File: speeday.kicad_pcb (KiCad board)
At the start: 4 copper layers, 100 x 100 mm, 238 parts, among them IC1 Trig Cond Socket, IC10 VNL5090N3-E, IC2 LM3940IMP-3.3_NOPB, IC3 VNL5090N3-E, IC4 VNL5090N3-E, IC5 VNL5090N3-E, IC6 VNL5090N3-E, IC7 VNL5090N3-E, IC8 VNL5090N3-E, IC9 VNL5090N3-E, J1 Conn_01x04, J10 Conn_02x02_Counter_Clockwise, J11 Conn_02x02_Counter_Clockwise, J12 Conn_02x02_Counter_Clockwise, J13 Conn_02x02_Counter_Clockwise, J14 Conn_02x02_Counter_Clockwise, J15 Conn_01x02, J16 Conn_01x02, J17 Conn_01x02, J18 Conn_01x02, J19 Conn_01x01, J2 Micro_SD_Card, J20 Conn_01x01, J21 Conn_01x01, J22 Conn_01x01, J23 Conn_01x02, J24 Conn_01x02, J25 Conn_01x08, J26 Conn_01x08, J27 Conn_01x04, J3 Conn_01x04, J4 Conn_01x02, J5 Conn_01x04, J6 Screw_Terminal_01x02, J7 Conn_02x02_Counter_Clockwise, J8 Conn_02x02_Counter_Clockwise, J9 Conn_02x02_Counter_Clockwise, P1 USB_C_Plug_USB2.0, Q1 SSM3K357R, Q2 SSM3K357R, Q3 SSM3K357R, Q4 SSM3K357R, SW1 SW_DIP_x01, SW2 SW_DIP_x01, SW3 SW_SPDT, U11 MCP2551-I-SN, U16 IXDN602, U17 IXDN602, U18 LM2940S-5.0/NOPB, U2 TXB0108PW, U3 TXB0108PW, U4 W25Q16JVSS, U5 MPX4250, U6 SP720, U7 STM32F407VGTx, Y1 Crystal_GND23

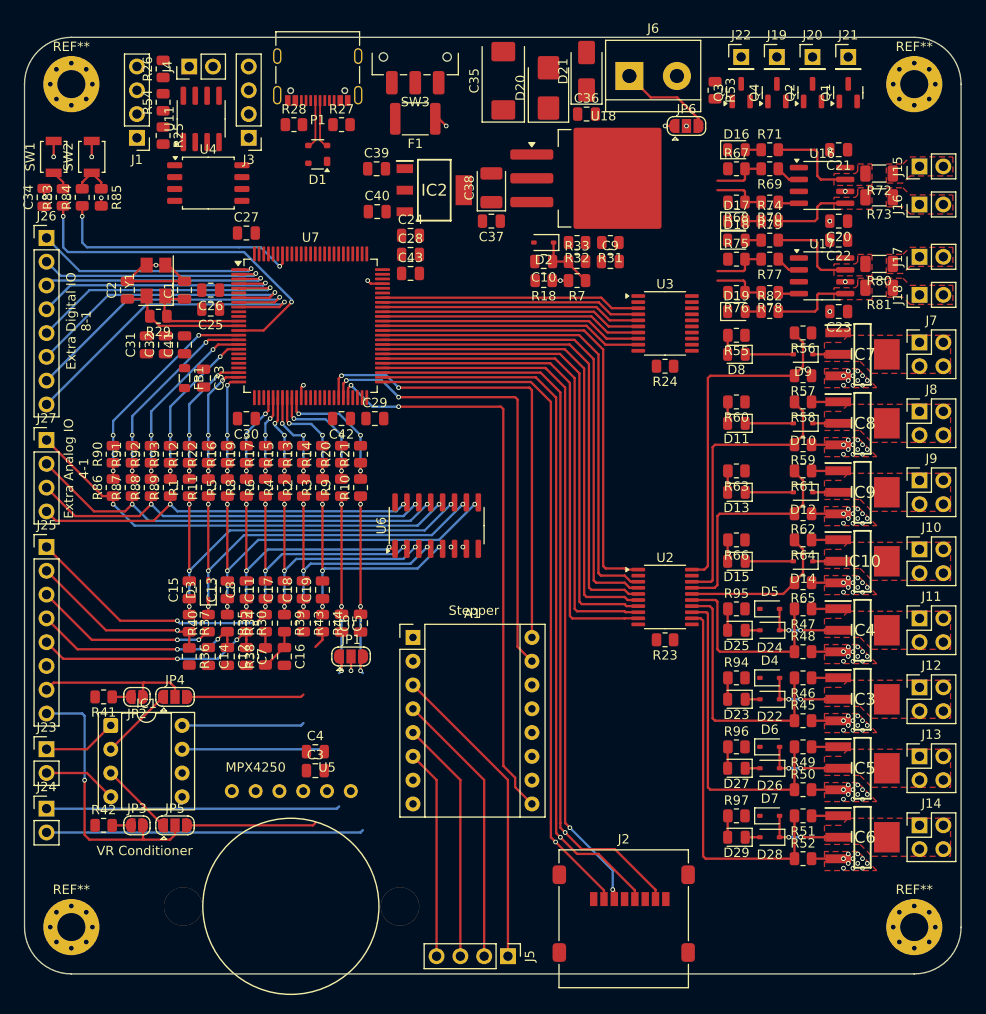
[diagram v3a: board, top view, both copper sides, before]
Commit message: Update from Speeduino Discord suggestions (thanks to Detonator)
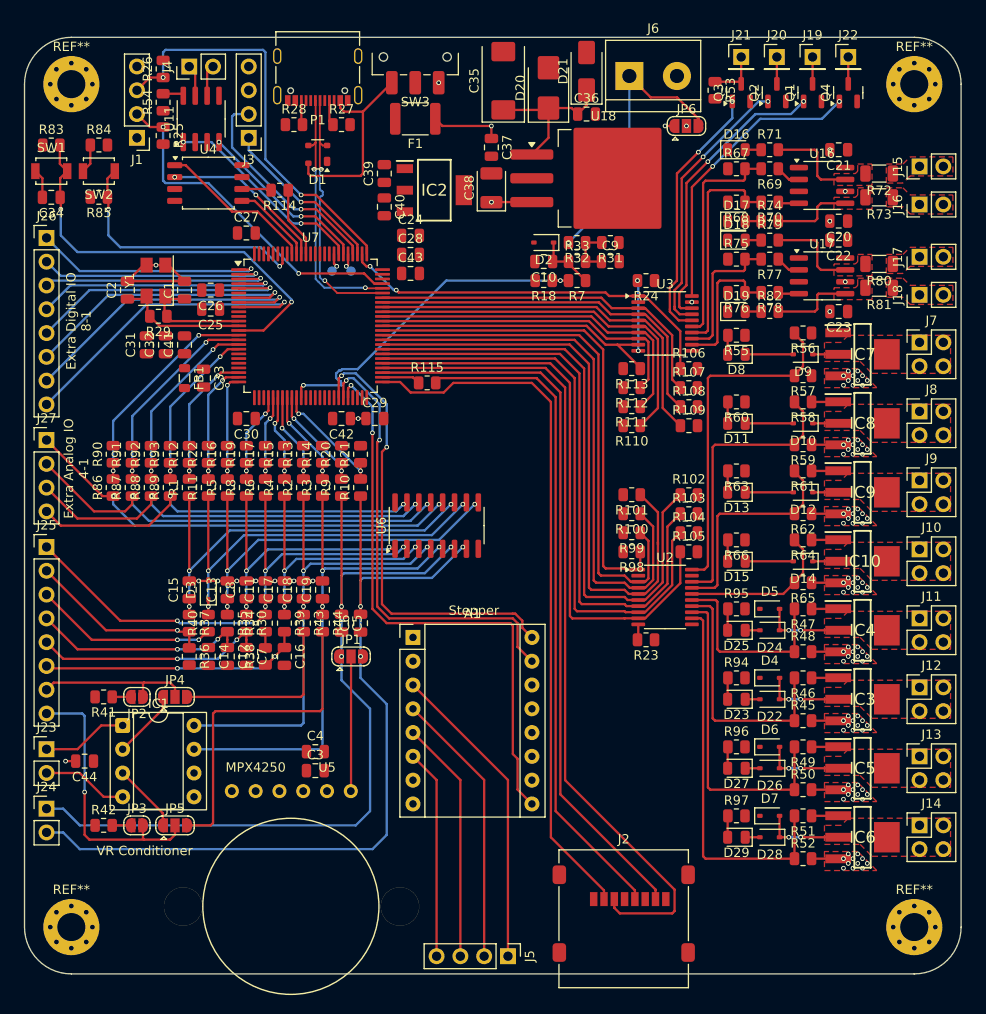
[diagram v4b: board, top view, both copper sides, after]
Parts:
- added C44: 100nF, Capacitor_SMD:C_0805_2012Metric, F.Cu at (26.4, 97.3)
- added R100: 51k, Resistor_SMD:R_0805_2012Metric, F.Cu at (84.8, 70.9)
- added R101: 51k, Resistor_SMD:R_0805_2012Metric, F.Cu at (84.8, 68.8)
- added R102: 51k, Resistor_SMD:R_0805_2012Metric, F.Cu at (90.9, 68.8)
- added R103: 51k, Resistor_SMD:R_0805_2012Metric, F.Cu at (90.9, 70.9)
- added R104: 51k, Resistor_SMD:R_0805_2012Metric, F.Cu at (90.9, 72.9)
- added R105: 51k, Resistor_SMD:R_0805_2012Metric, F.Cu at (90.9, 74.9)
- added R106: 51k, Resistor_SMD:R_0805_2012Metric, F.Cu at (90.9, 55.4)
- added R107: 51k, Resistor_SMD:R_0805_2012Metric, F.Cu at (90.9, 57.4)
- added R108: 51k, Resistor_SMD:R_0805_2012Metric, F.Cu at (90.9, 59.4)
- added R109: 51k, Resistor_SMD:R_0805_2012Metric, F.Cu at (90.9, 61.5)
- added R110: 51k, Resistor_SMD:R_0805_2012Metric, F.Cu at (84.8, 61.5)
- added R111: 51k, Resistor_SMD:R_0805_2012Metric, F.Cu at (84.8, 59.4)
- added R112: 51k, Resistor_SMD:R_0805_2012Metric, F.Cu at (84.8, 57.4)
- added R113: 51k, Resistor_SMD:R_0805_2012Metric, F.Cu at (84.8, 55.4)
- added R114: 22R, Resistor_SMD:R_0805_2012Metric, F.Cu at (47.2, 36.3)
- added R115: 22R, Resistor_SMD:R_0805_2012Metric, F.Cu at (63.0, 56.9)
- added R98: 51k, Resistor_SMD:R_0805_2012Metric, F.Cu at (84.8, 74.9)
- added R99: 51k, Resistor_SMD:R_0805_2012Metric, F.Cu at (84.8, 72.9)
- added TP1: TestPoint, TestPoint:TestPoint_Pad_D1.0mm, B.Cu at (52.8, 45.0)
- added TP2: TestPoint, TestPoint:TestPoint_Pad_D1.0mm, B.Cu at (54.9, 45.0)
- C10, C11, C13, C15, C17, C8: value 0.22uF -> 220nF
- C12, C14, C16, C19, C36, C37, C7, C9: value 0.1uF -> 100nF
- C18, C3: value 0.01uF -> 100nF
- C34: value C -> 100nF
- R84: value 10k -> 1k
- moved J21 11.4 mm to (96.5, 22.1)
- moved J22 11.4 mm to (108.0, 22.1)
- moved R24 9.37 mm to (86.4, 46.0)
- moved C37 7.87 mm to (69.8, 31.8), turned to -90 degrees
- moved Q4 7.62 mm to (108.0, 25.9)
- moved R84 5.86 mm to (27.9, 31.5), turned to 0 degrees
- moved R83 5.73 mm to (22.9, 31.5), turned to 0 degrees
- moved J19 3.81 mm to (104.1, 22.1)
- moved J20 3.81 mm to (100.3, 22.1)
- moved Q1 3.81 mm to (104.1, 25.9)
- moved Q2 3.81 mm to (100.3, 25.9)
- moved R23 2.03 mm to (86.4, 84.3)
- moved SW2 1.70 mm to (27.9, 34.3), turned to 180 degrees
- moved SW1 1.55 mm to (22.9, 34.3), turned to 0 degrees
- moved IC1 1.27 mm to (30.5, 93.5)
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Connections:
- C37 pad 1: 5V-REGULATOR -> +5V
- J2 pad 5: MCU-SPI-SD-CLK -> Net-(J2-CLK)
- R32 pad 2: +12V -> RAW-BAT
- R7 pad 1: RAW-BAT -> RAW-BAT-REF
- R83 pad 1: MCU_RESET -> +3.3V
- R83 pad 2: Net-(R83-Pad2) -> MCU_RESET
- R84 pad 1: MCU_BOOT -> Net-(R84-Pad1)
- R84 pad 2: Net-(R84-Pad2) -> +3.3V
- R85 pad 1: Net-(R84-Pad2) -> MCU_BOOT
- SW1 pad 1: Net-(R83-Pad2) -> GND
- SW1 pad 2: GND -> MCU_RESET
- SW2 pad 1: Net-(R84-Pad2) -> MCU_BOOT
- SW2 pad 2: +3.3V -> Net-(R84-Pad1)
- U3 pad 16: FAN-TRIG -> TACHO-TRIG
- U3 pad 18: TACHO-TRIG -> FAN-TRIG
- U3 pad 3: MCU-TACHO-TRIG-D -> MCU-FAN-TRIG-D
- U3 pad 5: MCU-FAN-TRIG-D -> MCU-TACHO-TRIG-D
- U4 pad 6: MCU-SPI-FLASH-CLK -> Net-(U4-CLK)
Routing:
- net MCU-SPI-SD-CLK: track 77.8 -> 4.11 mm, vias 1 -> 0
- net Net-(J2-CLK): track 0.00 -> 71.0 mm
- net MCU-SWD-CLK: track 0.00 -> 44.1 mm, vias 0 -> 2
- net MCU-LC-TRIG-D: track 0.00 -> 41.9 mm, vias 0 -> 2
- net RAW-BARO-IN: track 55.8 -> 91.5 mm, vias 4 -> 3
- net MCU-SWD-IO: track 1.71 -> 37.1 mm, vias 1 -> 2
- net RAW-MAP-IN: track 53.3 -> 88.6 mm, vias 4 -> 3
- net MCU-BAT-REF-IN-A: track 3.15 -> 37.0 mm
- net LC-TRIG: track 0.00 -> 31.2 mm, vias 0 -> 2
- net FAN-TRIG: track 0.00 -> 31.0 mm, vias 0 -> 2
- net FUELPUMP-TRIG: track 0.00 -> 29.0 mm, vias 0 -> 2
- net TACHO-TRIG: track 0.00 -> 27.9 mm, vias 0 -> 2
- net COOLANT-IN: track 4.50 -> 29.5 mm, vias 0 -> 2
- net MCU-UART-BT-RX: track 0.00 -> 23.3 mm, vias 0 -> 1
- net MCU-USB-D-: track 5.22 -> 27.6 mm, vias 0 -> 2
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
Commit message: Fully connect all components
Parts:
- removed C11, C13, C15, C17: 220nF, Capacitor_SMD:C_0805_2012Metric
- removed D1: SP0503BAHT, Package_TO_SOT_SMD:SOT-143
- removed IC2: LM3940IMP-3.3_NOPB, Misc:SOT230P700X180-4N
- removed R1, R11: 5k, Resistor_SMD:R_0805_2012Metric
- removed R114, R115: 22R, Resistor_SMD:R_0805_2012Metric
- removed R12, R22: 1k, Resistor_SMD:R_0805_2012Metric
- removed R23, R24: R, Resistor_SMD:R_0805_2012Metric
- removed R29: 1M, Resistor_SMD:R_0805_2012Metric
- removed REF** (x4): MountingHole_3mm_Pad_Via, MountingHole:MountingHole_3mm_Pad_Via
- removed SW3: SW_SPDT, Button_Switch_SMD:SW_SPDT_CK_JS102011SAQN
- removed U4: W25Q16JVSS, Package_SO:SOIC-8_5.3x5.3mm_P1.27mm
- removed Y1: Crystal_GND23, Crystal:Crystal_SMD_5032-4Pin_5.0x3.2mm
- added C46: 100nF, Capacitor_SMD:C_0805_2012Metric, F.Cu at (82.8, 46.0)
- added C47: 100nF, Capacitor_SMD:C_0805_2012Metric, F.Cu at (90.4, 84.3)
- added C48: 100nF, Capacitor_SMD:C_0805_2012Metric, F.Cu at (82.8, 84.3)
- added C49: 100nF, Capacitor_SMD:C_0805_2012Metric, F.Cu at (90.4, 46.0)
- added C50: 100nF, Capacitor_SMD:C_0805_2012Metric, F.Cu at (85.1, 103.4)
- added C51: 22µF, Capacitor_SMD:C_0805_2012Metric, F.Cu at (85.1, 101.3)
- added C52: 100nF, Capacitor_SMD:C_0805_2012Metric, F.Cu at (32.8, 39.1)
- added C53: 100nF, Capacitor_SMD:C_0805_2012Metric, F.Cu at (56.4, 34.5)
- added C59: 22µF, Capacitor_SMD:C_0805_2012Metric, F.Cu at (32.8, 41.1)
- added C62: 470pF, Capacitor_SMD:C_0805_2012Metric, F.Cu at (58.4, 34.5)
- added C64: 12pF, Capacitor_SMD:C_0805_2012Metric, F.Cu at (35.1, 48.8)
- added C65: 12pF, Capacitor_SMD:C_0805_2012Metric, F.Cu at (35.1, 52.3)
- added D30: D_TVS, Diode_SMD:D_SMB, F.Cu at (66.3, 25.4)
- added D31: D_Schottky, Diode_SMD:D_SOD-323, F.Cu at (57.4, 31.8)
- added D32: SP0503BAHT, Package_TO_SOT_SMD:SOT-143, F.Cu at (51.3, 32.5)
- added IC11: LM3940IMP-3.3_NOPB, Misc:SOT230P700X180-4N, F.Cu at (63.8, 36.3)
- added NT1: NetTie_2, NetTie:NetTie-2_SMD_Pad0.5mm, F.Cu at (66.3, 31.2)
- added R116: 4.7k, Resistor_SMD:R_0805_2012Metric, F.Cu at (32.8, 37.1)
- added R117: 4.7k, Resistor_SMD:R_0805_2012Metric, F.Cu at (46.7, 34.3)
- added R118: 4.7k, Resistor_SMD:R_0805_2012Metric, F.Cu at (40.1, 40.9)
- added R119: 4.7k, Resistor_SMD:R_0805_2012Metric, F.Cu at (32.8, 35.1)
- added R120: 4.7k, Resistor_SMD:R_0805_2012Metric, F.Cu at (70.1, 58.2)
- added R121: 4.7k, Resistor_SMD:R_0805_2012Metric, F.Cu at (74.9, 63.0)
- added R122: 4.7k, Resistor_SMD:R_0805_2012Metric, F.Cu at (70.1, 60.2)
- added R123: 4.7k, Resistor_SMD:R_0805_2012Metric, F.Cu at (72.9, 63.0)
- added R124: 4.7k, Resistor_SMD:R_0805_2012Metric, F.Cu at (36.6, 40.9)
- added R125: 1k, Resistor_SMD:R_0805_2012Metric, F.Cu at (48.0, 67.6)
- added R135: 1k, Resistor_SMD:R_0805_2012Metric, F.Cu at (39.9, 67.6)
- added R140: 2k, Resistor_SMD:R_0805_2012Metric, F.Cu at (48.0, 64.0)
- added R150: 2k, Resistor_SMD:R_0805_2012Metric, F.Cu at (39.9, 64.0)
- added R155: R, Resistor_SMD:R_0805_2012Metric, F.Cu at (86.4, 84.3)
- added R162: 22R, Resistor_SMD:R_0805_2012Metric, F.Cu at (46.7, 36.3)
- added R166: R, Resistor_SMD:R_0805_2012Metric, F.Cu at (86.4, 46.0)
- added R167: 22R, Resistor_SMD:R_0805_2012Metric, F.Cu at (75.9, 67.1)
- added R176: 1M, Resistor_SMD:R_0805_2012Metric, F.Cu at (37.1, 50.5)
- added U1: MCP6004, Package_SO:TSSOP-14_4.4x5mm_P0.65mm, F.Cu at (40.9, 78.0)
- added U10: W25Q16JVSS, Package_SO:SOIC-8_5.3x5.3mm_P1.27mm, F.Cu at (39.6, 35.6)
- added U12: TXB0108PW, Package_SO:TSSOP-20_4.4x6.5mm_P0.65mm, F.Cu at (88.4, 50.5)
- added U8: MCP6004, Package_SO:TSSOP-14_4.4x5mm_P0.65mm, F.Cu at (49.0, 83.6)
- added U9: TXB0108PW, Package_SO:TSSOP-20_4.4x6.5mm_P0.65mm, F.Cu at (88.4, 79.8)
- added Y2: Crystal_GND23, Crystal:Crystal_SMD_5032-4Pin_5.0x3.2mm, F.Cu at (31.0, 50.5)
- C1, C2: value 12pF -> 100nF
- C10: value 220nF -> 100nF
- C35: value 10uF -> 470nF
- C39: value 470pF -> 100nF
- C8: value 220nF -> 22µF
- R126: renamed from R2; value 5k -> 1k
- R127: renamed from R3; value 5k -> 1k
- R128: renamed from R4; value 5k -> 1k
- R129: renamed from R5; value 5k -> 1k
- R130: renamed from R6; value 5k -> 1k
- R131: renamed from R7; value 5k -> 1k
- R132: renamed from R8; value 5k -> 1k
- R133: renamed from R9; value 5k -> 1k
- R134: renamed from R10; value 5k -> 1k
- R141: renamed from R13; value 1k -> 2k
- R142: renamed from R14; value 1k -> 2k
- R143: renamed from R15; value 1k -> 2k
- R144: renamed from R16; value 1k -> 2k
- R145: renamed from R17; value 1k -> 2k
- R146: renamed from R18; value 1k -> 2k
- R147: renamed from R19; value 1k -> 2k
- R148: renamed from R20; value 1k -> 2k
- R149: renamed from R21; value 1k -> 2k
- R34: value 2.4k -> 2.49k
- R84: value 1k -> 470R
- R86, R87, R88, R89: value 5k -> 1k
- R90, R91, R92, R93: value 1k -> 2k
- U2: value TXB0108PW -> MCP6004; footprint Package_SO:TSSOP-20_4.4x6.5mm_P0.65mm -> Package_SO:TSSOP-14_4.4x5mm_P0.65mm
- U3: value TXB0108PW -> MCP6002-xMS; footprint Package_SO:TSSOP-20_4.4x6.5mm_P0.65mm -> Package_SO:TSSOP-8_4.4x3mm_P0.65mm
- moved U2 56.1 mm to (32.8, 72.4)
- moved C10 53.0 mm to (46.2, 88.1), turned to -90 degrees
- moved C39 51.1 mm to (30.0, 77.0), turned to -90 degrees
- moved U3 50.2 mm to (55.1, 88.1)
- moved D3 48.2 mm to (47.8, 31.5), turned to 0 degrees
- moved C1 43.1 mm to (50.0, 88.1), turned to -90 degrees
- moved C2 36.3 mm to (38.1, 82.5), turned to -90 degrees
- moved C8 31.8 mm to (61.5, 105.3)
- moved R44 25.6 mm to (38.1, 104.1), turned to 180 degrees
- moved R34 20.1 mm to (26.4, 77.0), turned to 180 degrees
- moved R38 19.3 mm to (26.4, 85.1), turned to 180 degrees
- moved C19 19.2 mm to (42.4, 95.8), turned to 0 degrees
- moved C16 17.8 mm to (30.0, 85.1), turned to 0 degrees
- moved C36 17.8 mm to (62.2, 27.9), turned to 180 degrees
- moved C18 16.5 mm to (42.4, 93.7), turned to 0 degrees
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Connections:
- A1 pad 8: +12V -> VBAT
- C1 pad 1: MCU-OSC-IN -> +5V
- C10 pad 1: RAW-BAT-REF -> +5V
- C18 pad 1: RAW-CRANK-IN -> CRANK-HZ-IN
- C19 pad 1: RAW-CAM-IN -> CAM-HZ-IN
- C2 pad 1: MCU-OSC-OUT -> +5V
- C36 pad 1: Net-(D20-K) -> 5V-REGULATOR
- C39 pad 1: GND -> +5V
- C39 pad 2: +5V -> GND
- C5 pad 1: RAW-MAP-IN -> MAP-HZ-IN
- C6 pad 2: RAW-BARO-IN -> BARO-HZ-IN
- C8 pad 1: RAW-O2 -> GND
- C8 pad 2: GND -> VBAT
- D2 pad 1: RAW-BAT-REF -> BAT-REF-HZ
- D21 pad 2: +12V -> VBAT
- D3 pad 1: RAW-CLUTCH -> MCU-UART-BT-RX
- D4 pad 1: +12V -> VBAT
- D5 pad 1: +12V -> VBAT
- D6 pad 1: +12V -> VBAT
- D7 pad 1: +12V -> VBAT
- IC1 pad 7: RAW-CAM-IN -> CAM-HZ-IN
- IC1 pad 8: RAW-CRANK-IN -> CRANK-HZ-IN
- J24 pad 1: RAW-MAP-IN -> MAP-HZ-IN
- J24 pad 2: RAW-BARO-IN -> BARO-HZ-IN
- J25 pad 1: RAW-FLEX-IN -> FLEX-HZ-IN
- J25 pad 2: IAT-IN -> CLUTCH-HZ-IN
- J25 pad 3: CLUTCH-IN -> TPS-IN
- J25 pad 4: TPS-IN -> O2-IN
- J25 pad 5: O2-IN -> COOLANT-IN
- J25 pad 6: COOLANT-IN -> IAT-IN
- J27 pad 1: RAW-EXTRA-GPIO-9-A -> EXTRA-GPIO-12-HZ-A
- J27 pad 2: RAW-EXTRA-GPIO-10-A -> EXTRA-GPIO-11-HZ-A
- J27 pad 3: RAW-EXTRA-GPIO-11-A -> EXTRA-GPIO-10-HZ-A
- J27 pad 4: RAW-EXTRA-GPIO-12-A -> EXTRA-GPIO-9-HZ-A
- J6 pad 1: RAW-BAT -> VBAT
- JP1 pad 1: RAW-MAP-IN -> MAP-HZ-IN
- JP1 pad 3: RAW-BARO-IN -> BARO-HZ-IN
- JP6 pad 3: RAW-BAT -> VBAT
- P1 pad S1: unconnected-(P1-SHIELD-PadS1)_3 -> GND
- R126 pad 1: RAW-CRANK-IN -> CRANK-LZ
- R127 pad 1: RAW-CAM-IN -> CAM-LZ
- R128 pad 1: RAW-COOLANT -> COOLANT-LZ
- R129 pad 1: RAW-TPS -> TPS-LZ
- R130 pad 1: RAW-FLEX-IN -> FLEX-LZ
- R131 pad 1: RAW-BAT-REF -> BAT-REF-HZ
- R132 pad 1: RAW-O2 -> O2-LZ
- R133 pad 1: RAW-MAP-IN -> MAP-LZ
- R134 pad 1: RAW-BARO-IN -> MCU-BARO-IN-A
- R134 pad 2: MCU-BARO-IN-A -> BARO-LZ
- R30 pad 1: RAW-O2 -> O2-HZ
- R32 pad 2: RAW-BAT -> VBAT
- R33 pad 1: RAW-BAT-REF -> BAT-REF-HZ
- R34 pad 1: +5VA -> FLEX-HZ-IN
- R34 pad 2: RAW-FLEX-IN -> +5VA
- R35 pad 1: RAW-TPS -> TPS-HZ
- R37 pad 1: RAW-IAT -> IAT-HZ
- R39 pad 1: RAW-COOLANT -> COOLANT-HZ
- R40 pad 1: CLUTCH-IN -> CLUTCH-HZ-IN
- R40 pad 2: RAW-CLUTCH -> CLUTCH-HZ
- R43 pad 1: RAW-CRANK-IN -> CRANK-HZ-IN
- R44 pad 1: RAW-CAM-IN -> CAM-HZ-IN
- R53 pad 2: +12V -> VBAT
- R55 pad 1: +12V -> VBAT
- R60 pad 1: +12V -> VBAT
- R63 pad 1: +12V -> VBAT
- R66 pad 1: +12V -> VBAT
- R86 pad 1: RAW-EXTRA-GPIO-9-A -> EXTRA-GPIO-9-LZ-A
- R87 pad 1: RAW-EXTRA-GPIO-10-A -> EXTRA-GPIO-10-LZ-A
- R88 pad 1: RAW-EXTRA-GPIO-11-A -> EXTRA-GPIO-11-LZ-A
- R89 pad 1: RAW-EXTRA-GPIO-12-A -> EXTRA-GPIO-12-LZ-A
- R94 pad 2: +12V -> VBAT
- R95 pad 2: +12V -> VBAT
- R96 pad 2: +12V -> VBAT
- R97 pad 2: +12V -> VBAT
- U2 pad 1: MCU-INJ-1-TRIG-D -> EXTRA-GPIO-10-LZ-A
- U2 pad 10: Net-(U2-OE) -> EXTRA-GPIO-11-HZ-A
- U2 pad 12: HC2-TRIG -> EXTRA-GPIO-12-HZ-A
- U2 pad 13: HC1-TRIG -> EXTRA-GPIO-12-LZ-A
- U2 pad 14: BOOST-TRIG -> EXTRA-GPIO-12-LZ-A
- U2 pad 2: +3.3V -> EXTRA-GPIO-10-LZ-A
- U2 pad 3: MCU-INJ-2-TRIG-D -> EXTRA-GPIO-10-HZ-A
- U2 pad 4: MCU-INJ-3-TRIG-D -> +5V
- U2 pad 5: MCU-INJ-4-TRIG-D -> EXTRA-GPIO-9-HZ-A
- U2 pad 6: MCU-IDLE-TRIG-D -> EXTRA-GPIO-9-LZ-A
- U2 pad 7: MCU-BOOST-TRIG-D -> EXTRA-GPIO-9-LZ-A
- U2 pad 8: MCU-HC-1-TRIG-D -> EXTRA-GPIO-11-LZ-A
- U2 pad 9: MCU-HC-2-TRIG-D -> EXTRA-GPIO-11-LZ-A
- U3 pad 1: MCU-LC-TRIG-D -> MAP-LZ
- U3 pad 2: +3.3V -> MAP-LZ
- U3 pad 3: MCU-FAN-TRIG-D -> MAP-HZ-IN
- U3 pad 4: MCU-FUELPUMP-TRIG-D -> GND
- U3 pad 5: MCU-TACHO-TRIG-D -> BARO-HZ-IN
- U3 pad 6: MCU-IGN-1-TRIG-D -> BARO-LZ
- U3 pad 7: MCU-IGN-2-TRIG-D -> BARO-LZ
- U3 pad 8: MCU-IGN-3-TRIG-D -> +5V
- U6 pad 1: RAW-O2 -> MAP-HZ-IN
- U6 pad 10: RAW-CLUTCH -> CLUTCH-HZ
- U6 pad 11: RAW-IAT -> FLEX-HZ-IN
- U6 pad 12: RAW-EXTRA-GPIO-9-A -> EXTRA-GPIO-9-HZ-A
- U6 pad 13: RAW-EXTRA-GPIO-10-A -> EXTRA-GPIO-10-HZ-A
- U6 pad 14: RAW-EXTRA-GPIO-11-A -> EXTRA-GPIO-11-HZ-A
- U6 pad 15: RAW-EXTRA-GPIO-12-A -> EXTRA-GPIO-12-HZ-A
- U6 pad 2: RAW-FLEX-IN -> BARO-HZ-IN
- U6 pad 3: RAW-COOLANT -> CAM-HZ-IN
- U6 pad 4: RAW-CRANK-IN -> CRANK-HZ-IN
- U6 pad 5: RAW-CAM-IN -> IAT-HZ
- U6 pad 6: RAW-MAP-IN -> COOLANT-HZ
- U6 pad 7: RAW-BARO-IN -> O2-HZ
- U6 pad 9: RAW-TPS -> TPS-HZ
- U7 pad 15: MCU-EXTRA-GPIO-9-A -> MCU-EXTRA-GPIO-10-A
- U7 pad 16: MCU-EXTRA-GPIO-10-A -> MCU-EXTRA-GPIO-9-A
- U7 pad 23: MCU-IAT-IN-A -> MCU-FLEX-IN-A
- U7 pad 25: MCU-TPS-IN-A -> MCU-O2-IN-A
- U7 pad 29: MCU-O2-IN-A -> MCU-TPS-IN-A
- U7 pad 30: MCU-FLEX-IN-A -> MCU-CLT-IN-A
- U7 pad 31: MCU-CLT-IN-A -> MCU-IAT-IN-A
- U7 pad 32: MCU-CRANK-IN-A -> MCU-CAM-IN-A
- U7 pad 33: MCU-CAM-IN-A -> MCU-CRANK-IN-A
- U7 pad 67: MCU-FAN-TRIG-D -> MCU-TACHO-TRIG-D
- U7 pad 69: MCU-TACHO-TRIG-D -> MCU-FAN-TRIG-D
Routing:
- net +3.3V: track 1.66 -> 260.8 mm, vias 1 -> 17
- net GND: track 52.0 -> 300.8 mm, vias 97 -> 172
- net +5V: track 27.2 -> 230.2 mm, vias 3 -> 16
- net VBAT: track 0.00 -> 179.7 mm, vias 0 -> 11
- net +5VA: track 1.73 -> 127.4 mm, vias 0 -> 8
- net RAW-BARO-IN: track 91.5 -> 0.00 mm, vias 3 -> 0
- net RAW-MAP-IN: track 88.6 -> 0.00 mm, vias 3 -> 0
- net BARO-HZ-IN: track 0.00 -> 70.3 mm, vias 0 -> 3
- net MAP-HZ-IN: track 0.00 -> 69.3 mm, vias 0 -> 3
- net RAW-FLEX-IN: track 56.8 -> 0.00 mm, vias 5 -> 0
- net RAW-CAM-IN: track 56.2 -> 0.00 mm, vias 3 -> 0
- net RAW-CRANK-IN: track 52.4 -> 0.00 mm, vias 3 -> 0
- net FLEX-HZ-IN: track 0.00 -> 48.5 mm, vias 0 -> 3
- net RAW-EXTRA-GPIO-9-A: track 47.6 -> 0.00 mm, vias 2 -> 0
- net EXTRA-GPIO-9-HZ-A: track 0.00 -> 46.9 mm, vias 0 -> 2
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- added copper zone on F.Cu, net Vdrive
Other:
- board text removed: "Extra Analog IO 4-1"
- board text removed: "Extra Digital IO 8-1"
- board text removed: "Stepper"

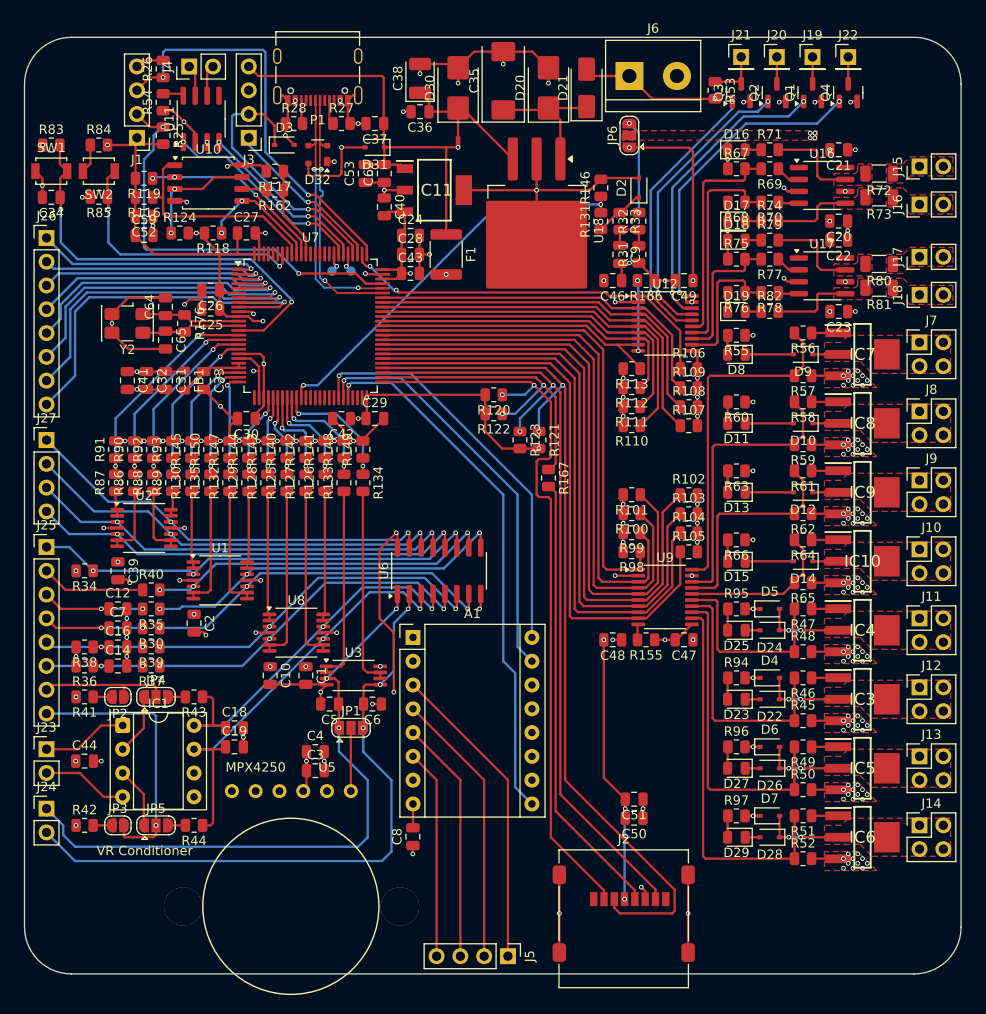
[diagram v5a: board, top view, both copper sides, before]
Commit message: Fix power traces width and add logo
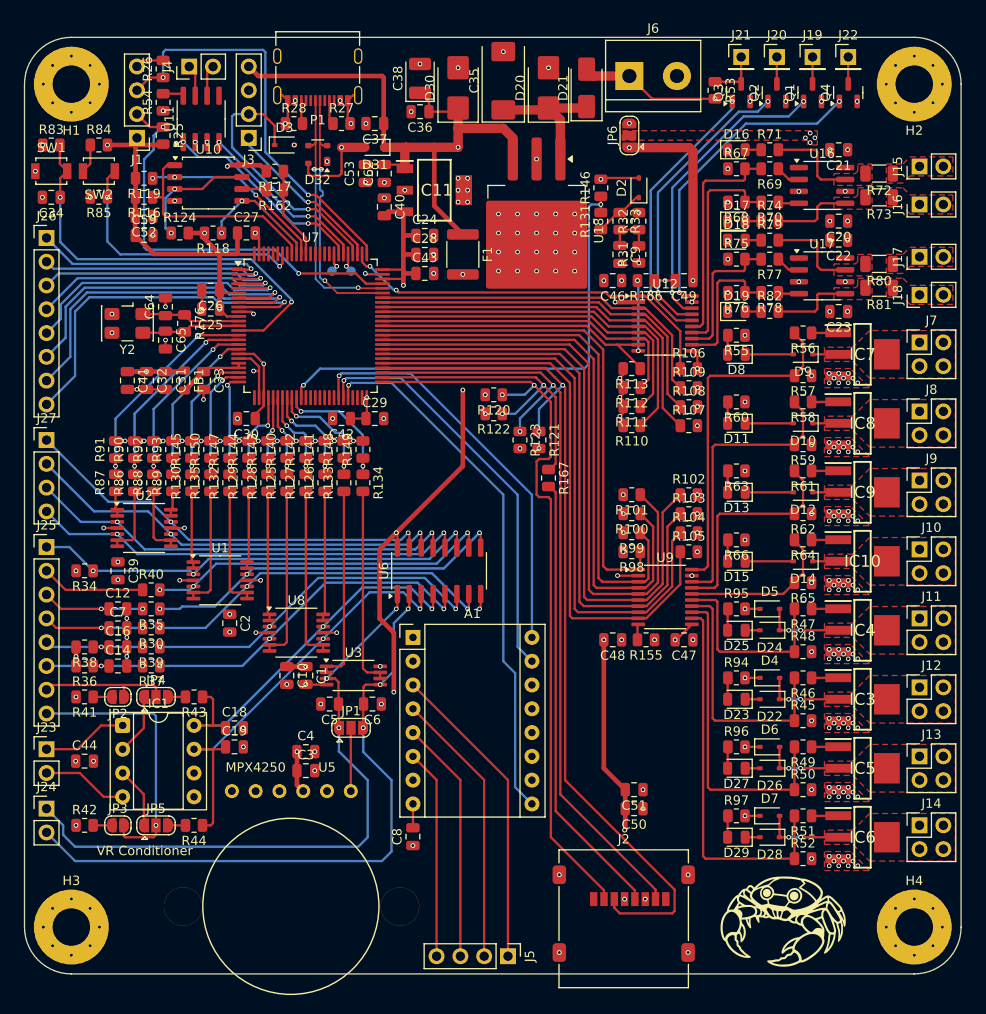
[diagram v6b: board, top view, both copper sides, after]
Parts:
- added G***: LOGO, Images:Logo_small, F.Cu at (101.0, 114.0)
- added H1: MountingHole_Pad, MountingHole:MountingHole_4mm_Pad, F.Cu at (25.0, 25.0)
- added H2: MountingHole_Pad, MountingHole:MountingHole_4mm_Pad, F.Cu at (115.0, 25.0)
- added H3: MountingHole_Pad, MountingHole:MountingHole_4mm_Pad, F.Cu at (25.0, 115.0)
- added H4: MountingHole_Pad, MountingHole:MountingHole_4mm_Pad, F.Cu at (115.0, 115.0)
- moved C2 3.81 mm to (41.9, 82.5)
- moved F1 1.78 mm to (66.8, 43.2)
- moved C10 1.78 mm to (48.0, 88.1)
- moved C24 1.52 mm to (62.7, 41.1)
- moved C28 1.52 mm to (62.7, 43.2)
- moved C43 1.52 mm to (62.7, 45.2)
- moved C3 1.02 mm to (50.0, 98.3)
- moved C4 1.02 mm to (50.0, 96.3)
- moved C50 1.02 mm to (85.1, 102.4)
- moved C51 1.02 mm to (85.1, 100.3)
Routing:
- net GND: track 300.8 -> 91.9 mm, vias 172 -> 266
- net VBAT: track 179.7 -> 169.7 mm
- net MCU-BAT-REF-IN-A: track 43.0 -> 52.8 mm
- net +5V: track 230.2 -> 239.3 mm, vias 16 -> 15
- net +3.3V: track 260.8 -> 263.3 mm, vias 17 -> 19
- net MCU-CAM-IN-A: track 11.3 -> 10.7 mm
- net MCU-TPS-IN-A: track 9.91 -> 10.5 mm
- net Net-(U10-~{HOLD}/~{RESET}/IO_{3}): track 12.6 -> 13.1 mm
- net +5VA: track 127.4 -> 127.7 mm, vias 8 -> 9
- added copper zone on In2.Cu, net 5V-USB

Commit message: Updated reference layout
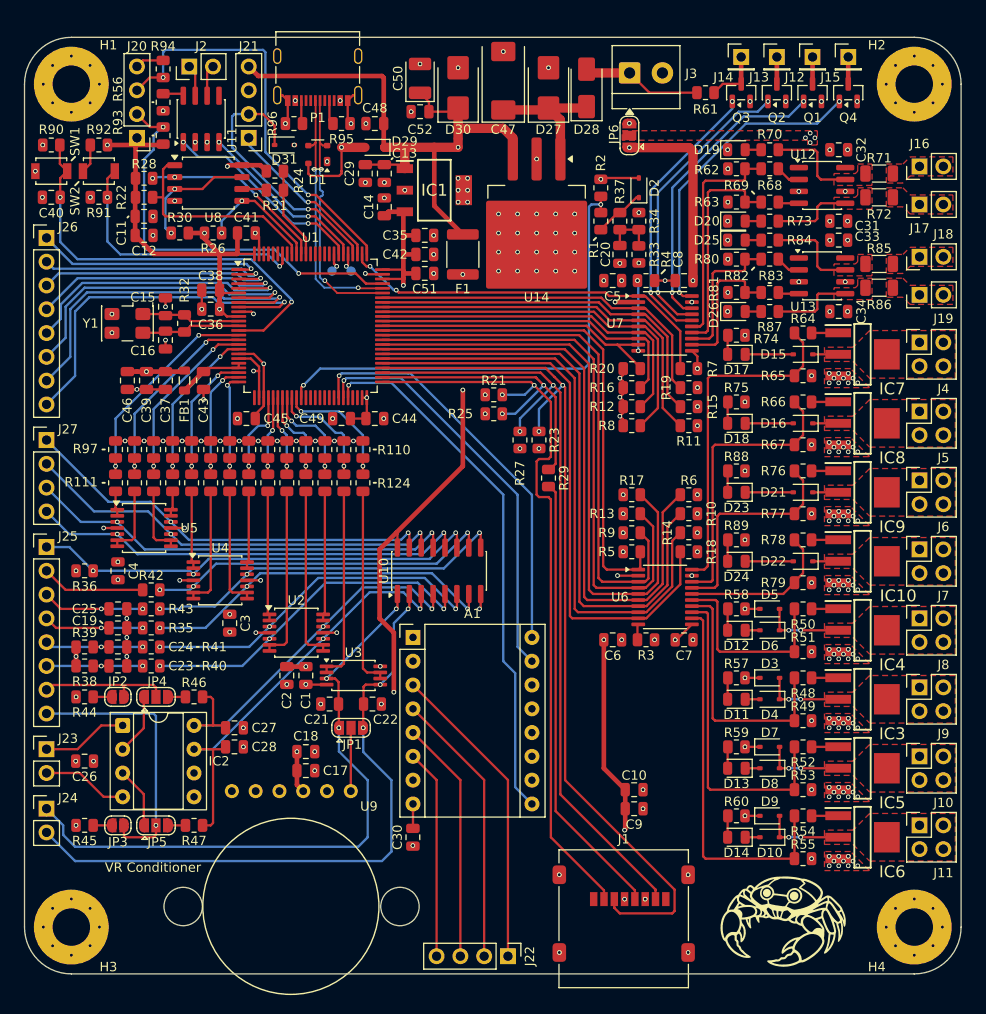
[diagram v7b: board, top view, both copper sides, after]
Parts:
- J3: renamed from J6; footprint TerminalBlock:TerminalBlock_bornier-2_P5.08mm -> TerminalBlock_MetzConnect:TerminalBlock_MetzConnect_Type059_RT06302HBWC_1x02_P3.50mm_Horizontal
- moved R61 1.05 mm to (92.7, 25.9), turned to 180 degrees
- moved J3 0.33 mm to (84.6, 23.8)
- moved C30 0.07 mm to (61.5, 105.4)
- renumbered C51 to C10, C52 to C11, C59 to C12, C62 to C13, C40 to C14, C64 to C15, C65 to C16, C3 to C17, C4 to C18, C7 to C19, C10 to C2, C9 to C20, C5 to C21, C6 to C22, C14 to C23, C16 to C24, C12 to C25, C44 to C26, C18 to C27, C19 to C28, C53 to C29, C2 to C3, C8 to C30, C20 to C31, C21 to C32, C22 to C33, C23 to C34, C24 to C35, C25 to C36, C31 to C37, C26 to C38, C32 to C39, C39 to C4, C34 to C40, C27 to C41, C28 to C42, C33 to C43, C29 to C44, C30 to C45, C41 to C46, C35 to C47, C37 to C48, C42 to C49, C46 to C5, C38 to C50, C43 to C51, C36 to C52, C48 to C6, C47 to C7, C49 to C8, C50 to C9, D32 to D1, D28 to D10, D23 to D11, D25 to D12, D27 to D13, D29 to D14, D9 to D15, D10 to D16, D8 to D17, D11 to D18, D16 to D19, D17 to D20, D12 to D21, D14 to D22, D13 to D23, D15 to D24, D18 to D25, D19 to D26, D20 to D27, D21 to D28, D31 to D29, D4 to D3, D3 to D31, D22 to D4, D24 to D6, D6 to D7, D26 to D8, D7 to D9, IC11 to IC1, IC1 to IC2, J2 to J1, J13 to J10, J14 to J11, J19 to J12, J20 to J13, J21 to J14, J22 to J15, J15 to J16, J16 to J17, J17 to J18, J18 to J19, J4 to J2, J1 to J20, J3 to J21, J5 to J22, J7 to J4, J8 to J5, J9 to J6, J10 to J7, J11 to J8, J12 to J9, R131 to R1, R103 to R10, R93 to R100, R145 to R101, R150 to R102, R147 to R103, R144 to R104, R143 to R105, R140 to R106, R142 to R107, R141 to R108, R148 to R109, R107 to R11, R149 to R110, R87 to R111, R86 to R112, R88 to R113, R89 to R114, R130 to R115, R135 to R116, R132 to R117, R129 to R118, R128 to R119, R111 to R12, R125 to R120, R127 to R121, R126 to R122, R133 to R123, R134 to R124, R100 to R13, R104 to R14, R108 to R15, R112 to R16, R101 to R17, R105 to R18, R109 to R19, R146 to R2, R113 to R20, R120 to R21, R116 to R22, R121 to R23, R117 to R24, R122 to R25, R118 to R26, R123 to R27, R119 to R28, R167 to R29, R155 to R3, R124 to R30, R162 to R31, R176 to R32, R31 to R33, R32 to R34, R30 to R35, R34 to R36, R33 to R37, R36 to R38, R38 to R39, R166 to R4, R37 to R40, R39 to R41, R40 to R42, R35 to R43, R41 to R44, R42 to R45, R43 to R46, R44 to R47, R46 to R48, R45 to R49, R98 to R5, R47 to R50, R48 to R51, R49 to R52, R50 to R53, R51 to R54, R52 to R55, R54 to R56, R94 to R57, R95 to R58, R96 to R59, R102 to R6, R97 to R60, R53 to R61, R67 to R62, R68 to R63, R56 to R64, R57 to R65, R58 to R66, R59 to R67, R69 to R68, R70 to R69, R106 to R7, R71 to R70, R72 to R71, R73 to R72, R74 to R73, R55 to R74, R60 to R75, R61 to R76, R62 to R77, R64 to R78, R65 to R79, R110 to R8, R75 to R80, R76 to R81, R77 to R82, R78 to R83, R79 to R84, R80 to R85, R81 to R86, R82 to R87, R63 to R88, R66 to R89, R99 to R9, R83 to R90, R85 to R91, R84 to R92, R25 to R93, R26 to R94, R27 to R95, R28 to R96, R91 to R97, R90 to R98, R92 to R99, U7 to U1, U6 to U10, U16 to U12, U17 to U13, U18 to U14, U8 to U2, U1 to U4, U2 to U5, U9 to U6, U12 to U7, U10 to U8, U5 to U9, Y2 to Y1
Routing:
- net VBAT: track 169.7 -> 168.4 mm, vias 11 -> 10
- net +5VA: vias 9 -> 8
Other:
- board text added: "R110"
- board text added: "R111"
- board text added: "R124"
- board text added: "R97"
